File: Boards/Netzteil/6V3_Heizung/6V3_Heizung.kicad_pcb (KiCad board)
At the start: 2 copper layers, 36 parts, among them P1 6V3_AC, P2 12V_DC, P3 6V3_DC_1, P4 6V3_DC_2, Q3 IRF540N, Q4 IRF540N, U1 TL072

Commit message: Updated Layout
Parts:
- added REF**: EuroBoard_halb_Type-I_100mmX80mm_holes, EuroBoard_Outline:EuroBoard_halb_Type-I_100mmX80mm_holes, F.Cu at (59.7, 118.7)
- moved R4 42.0 mm to (110.5, 55.2), turned to 180 degrees
- moved C11 33.1 mm to (151.8, 70.5)
- moved C12 33.1 mm to (151.8, 85.7)
- moved R6 33.1 mm to (135.5, 68.3)
- moved R7 33.1 mm to (135.6, 75.2)
- moved R8 33.1 mm to (135.5, 87.9)
- moved R9 33.1 mm to (135.5, 81.3)
- moved C13 33.1 mm to (134.2, 71.6)
- moved C14 33.1 mm to (134.2, 84.6)
- moved C15 33.1 mm to (142.6, 71.6)
- moved C16 33.1 mm to (142.6, 84.6)
- moved P3 33.1 mm to (154.3, 55.9)
- moved P4 33.1 mm to (154.3, 100.3)
- moved R5 30.6 mm to (71.1, 102.2)
- moved Q4 23.7 mm to (131.4, 49.5)
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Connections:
- net Ref renamed /Reference
- net V_Unreg renamed /V_Unreg
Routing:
- net Net-(R2-Pad2): track 11.4 -> 72.9 mm
- net Net-(Q4-Pad1): track 56.5 -> 8.86 mm, vias 2 -> 0
- net Net-(C14-Pad1): track 97.1 -> 79.7 mm
- net Net-(Q3-Pad1): track 46.2 -> 59.6 mm
- net Net-(C11-Pad1): track 77.9 -> 67.7 mm
- net /Reference: track 45.2 -> 36.6 mm
- net Net-(C12-Pad1): track 75.9 -> 67.2 mm
- net /V_Unreg: track 135.3 -> 143.2 mm
- net Net-(R3-Pad2): track 19.6 -> 23.2 mm
- net Net-(C13-Pad1): track 73.0 -> 69.5 mm
- net +12V: track 53.7 -> 50.6 mm
- net Net-(C1-Pad1): track 36.6 -> 33.5 mm
- net Net-(C6-Pad1): track 6.40 -> 7.94 mm
- net Net-(C7-Pad1): track 3.81 -> 5.34 mm
- net Net-(C2-Pad2): track 32.6 -> 33.3 mm
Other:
- board outline added: 100 x 80 mm

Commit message: Work in Progress
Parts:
- moved C9 0.64 mm to (81.3, 53.3)
- turned D5 to 180 degrees
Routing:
- net GND: track 0.00 -> 20.8 mm, vias 0 -> 2
- net Net-(C13-Pad1): track 69.5 -> 66.0 mm
- net Net-(C14-Pad1): track 79.7 -> 77.1 mm
- net Net-(C12-Pad1): track 67.2 -> 65.1 mm
- net Net-(C2-Pad2): track 33.3 -> 31.4 mm
- net /Reference: track 36.6 -> 38.0 mm
- net Net-(R2-Pad2): track 72.9 -> 71.5 mm
- net +12V: track 50.6 -> 49.4 mm
- net Net-(C1-Pad1): track 33.5 -> 32.6 mm
- net Net-(C11-Pad1): track 67.7 -> 66.9 mm
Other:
- net class Default: via_dia 1 -> 1.5

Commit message: Work in Progress
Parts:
- moved R4 26.1 mm to (135.3, 63.5)
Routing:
- net /V_Unreg: track 143.1 -> 114.3 mm
- net Net-(Q4-Pad1): track 8.86 -> 22.0 mm
- net Net-(C12-Pad1): track 65.1 -> 68.2 mm
- net Net-(R2-Pad2): track 71.5 -> 69.4 mm, vias 0 -> 2
- net Net-(C13-Pad1): track 66.0 -> 67.6 mm
- net Net-(C11-Pad1): track 66.9 -> 67.9 mm
- net Net-(C14-Pad1): track 77.1 -> 76.5 mm
- added copper zone on B.Cu, net /V_Unreg

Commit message: Work in Progress
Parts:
- P2: footprint MiniUniversalMate-N-LokSockets_13Aug2012:MiniUniversalMate-N-LokSocket_2PinVertical_12Aug2012 -> Connectors_Molex:Molex_KK-6410-02_02x2.54mm_Straight
- moved R1 3.43 mm to (73.3, 88.4)
- moved R3 3.05 mm to (79.9, 102.2)
- moved R2 2.57 mm to (101.0, 100.6)
- moved D5 2.29 mm to (78.4, 88.4), turned to 90 degrees
- moved R5 2.16 mm to (73.3, 102.2)
- moved C6 1.94 mm to (97.2, 100.6)
- moved C7 1.55 mm to (83.4, 98.1)
- moved P2 0.64 mm to (64.8, 88.3)
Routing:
- net /Reference: track 38.0 -> 32.1 mm
- net GND: track 20.8 -> 26.5 mm
- net +12V: track 49.4 -> 53.6 mm
- net /V_Unreg: track 114.3 -> 111.1 mm
- net Net-(C13-Pad1): track 67.6 -> 70.0 mm
- net Net-(Q3-Pad1): track 59.6 -> 57.7 mm
- net Net-(C14-Pad1): track 76.5 -> 74.8 mm
- net Net-(R2-Pad2): track 69.4 -> 67.8 mm
- net Net-(C7-Pad1): track 5.34 -> 3.94 mm
- net Net-(C6-Pad1): track 7.69 -> 6.66 mm
- net Net-(R3-Pad2): track 23.6 -> 23.0 mm
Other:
- board text added: "Bot"
- board text added: "D. Walter v1.0"

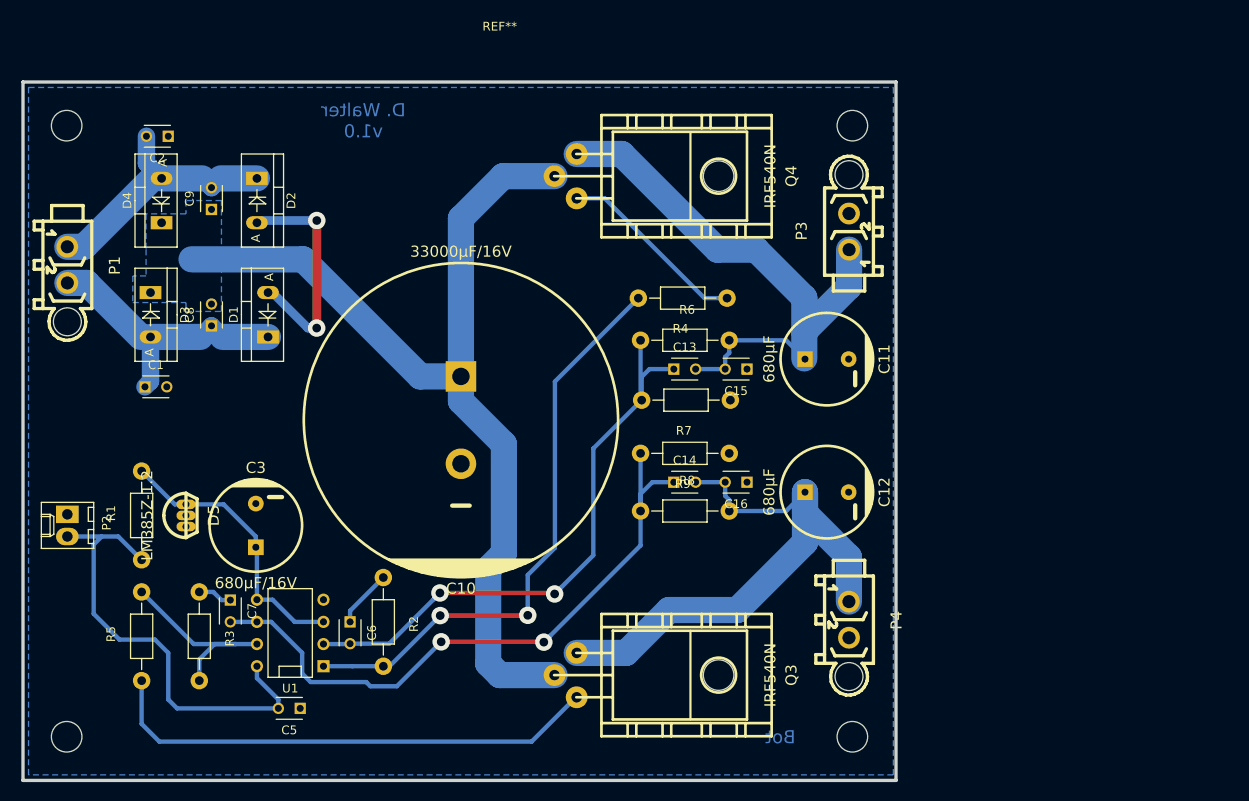
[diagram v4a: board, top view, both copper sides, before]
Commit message: Converted to Kicad 5.1 and Layout changes
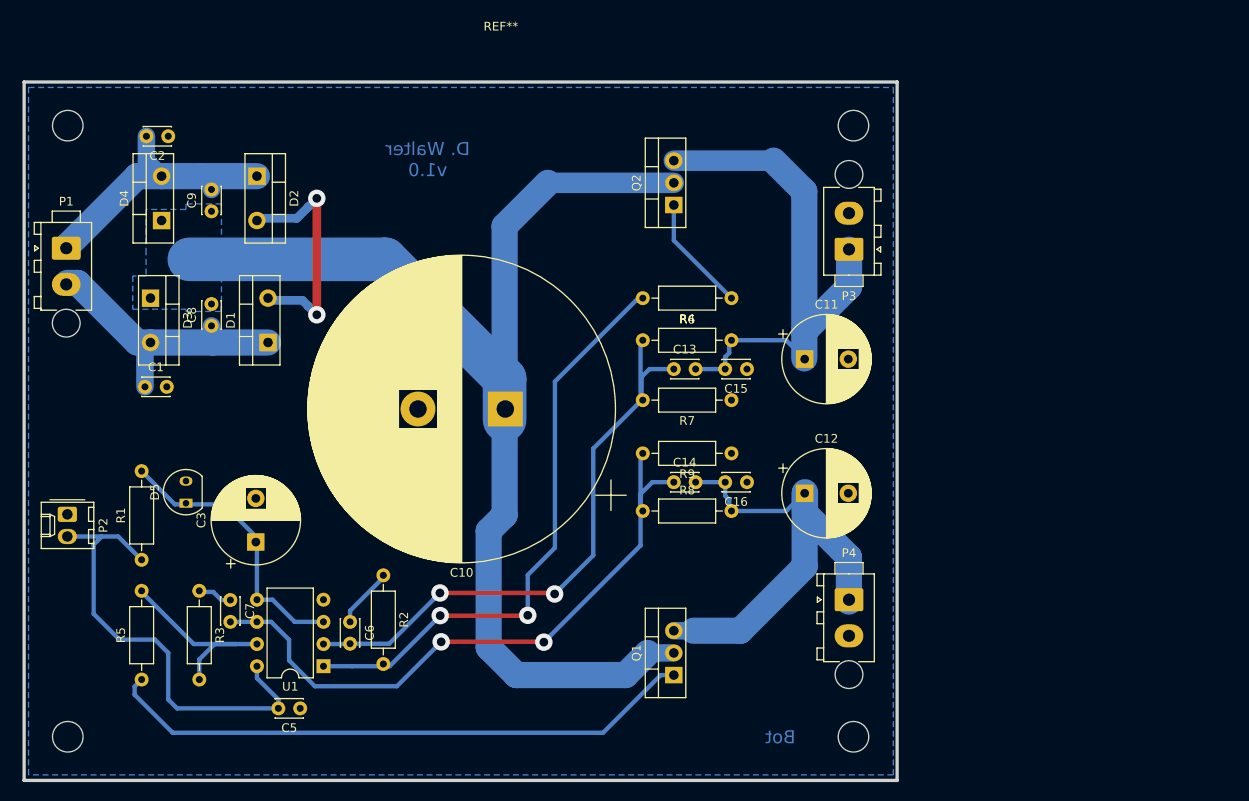
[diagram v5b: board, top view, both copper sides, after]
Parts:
- removed Q3, Q4: IRF540N, w_to:to220-horiz_5772
- added Q1: IRF540N, Package_TO_SOT_THT:TO-220-3_Vertical, F.Cu at (134.2, 106.7)
- added Q2: IRF540N, Package_TO_SOT_THT:TO-220-3_Vertical, F.Cu at (134.2, 52.8)
- C1, C13, C14, C15, C16, C2, C5, C6, C7, C8, C9: footprint Capacitors_ThroughHole:C_Disc_D3_P2.5 -> Capacitor_THT:C_Disc_D3.0mm_W2.0mm_P2.50mm
- C10: footprint w_capacitors:CP_35x40mm -> Capacitor_THT:CP_Radial_D35.0mm_P10.00mm_SnapIn
- C11, C12, C3: footprint w_capacitors:CP_10x16mm -> Capacitor_THT:CP_Radial_D10.0mm_P5.00mm
- D1, D2, D3, D4: footprint Diodes_ThroughHole:Diode_TO-220_Vertical -> Package_TO_SOT_THT:TO-220-2_Vertical
- D5: footprint w_to:to92_3_flat -> Package_TO_SOT_THT:TO-92-2
- P1, P3, P4: footprint MiniUniversalMate-N-LokSockets_13Aug2012:MiniUniversalMate-N-LokSocket_2PinVertical_12Aug2012 -> Connector_TE-Connectivity:TE_MATE-N-LOK_1-770866-x_1x02_P4.14mm_Vertical
- P2: footprint Connectors_Molex:Molex_KK-6410-02_02x2.54mm_Straight -> Connector_Molex:Molex_KK-254_AE-6410-02A_1x02_P2.54mm_Vertical
- R1, R2, R3, R4, R5, R6, R7, R8, R9: footprint Resistors_ThroughHole:Resistor_Horizontal_RM10mm -> Resistor_THT:R_Axial_DIN0207_L6.3mm_D2.5mm_P10.16mm_Horizontal
- U1: footprint Sockets_DIP:DIP-8__300 -> Package_DIP:DIP-8_W7.62mm
- moved R4 5.59 mm to (140.8, 63.5)
- moved U1 5.39 mm to (94.1, 105.7), turned to 180 degrees
- moved R2 5.33 mm to (101.0, 95.2)
- moved R9 5.33 mm to (140.8, 81.3)
- moved C10 5.24 mm to (114.9, 76.2)
- moved R3 5.21 mm to (79.9, 97.0)
- moved R7 5.21 mm to (140.8, 75.2)
- moved R1 5.08 mm to (73.3, 93.5)
- moved R5 4.95 mm to (73.3, 107.2)
- moved R6 4.83 mm to (130.7, 68.3)
- moved R8 4.83 mm to (130.7, 87.9)
- moved C12 2.54 mm to (149.2, 85.9), turned to 0 degrees
- moved C11 2.54 mm to (149.2, 70.5), turned to 0 degrees
- moved P4 2.29 mm to (154.3, 98.0), turned to 0 degrees
- moved P3 2.03 mm to (154.3, 57.9), turned to 180 degrees
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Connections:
- U1 pad 8: +12V -> (no net)
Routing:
- net /V_Unreg: track 111.1 -> 140.6 mm
- net Net-(C12-Pad1): track 68.2 -> 57.5 mm
- net Net-(Q1-Pad1): track 57.7 -> 68.4 mm
- net Net-(Q2-Pad1): track 22.0 -> 13.4 mm
- net Net-(C11-Pad1): track 67.9 -> 63.6 mm
- net Net-(C2-Pad2): track 31.4 -> 32.7 mm
- net GND: track 26.5 -> 27.7 mm
- net Net-(C1-Pad1): track 32.6 -> 33.1 mm

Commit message: Minor Layout changes
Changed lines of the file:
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@@
     (thickness 1.6)
     (drawings 2)
-    (tracks 170)
+    (tracks 172)
     (zones 0)
     (modules 37)
@@
   (segment (start 149.18448 67.31) (end 149.18448 51.26748) (width 3) (layer B.Cu) (net 9))
   (segment (start 145.669 47.752) (end 149.18448 51.26748) (width 3) (layer B.Cu) (net 9))
-  (segment (start 134.239 47.752) (end 145.669 47.752) (width 2.35) (layer B.Cu) (net 9))
+  (segment (start 136.652 47.752) (end 145.669 47.752) (width 3) (layer B.Cu) (net 9))
+  (segment (start 134.239 47.752) (end 136.652 47.752) (width 2.35) (layer B.Cu) (net 9))
   (segment (start 140.121 84.582) (end 140.121 86.15318) (width 0.5) (layer B.Cu) (net 10))
   (segment (start 140.121 86.15318) (end 140.584902 86.617082) (width 0.5) (layer B.Cu) (net 10))
@@
   (segment (start 114.855 55.2488) (end 114.855 77.47) (width 3) (layer B.Cu) (net 14))
   (segment (start 119.8118 50.292) (end 114.855 55.2488) (width 3) (layer B.Cu) (net 14))
-  (segment (start 134.239 50.292) (end 119.8118 50.292) (width 2.35) (layer B.Cu) (net 14))
   (segment (start 114.855 77.47) (end 114.855 88.345) (width 3) (layer B.Cu) (net 14))
   (segment (start 114.855 88.345) (end 113.03 90.17) (width 3) (layer B.Cu) (net 14))
@@
   (segment (start 134.239 104.14) (end 131.239 104.14) (width 2) (layer B.Cu) (net 14))
   (segment (start 131.239 104.14) (end 128.699 106.68) (width 3) (layer B.Cu) (net 14))
+  (segment (start 131.064 50.292) (end 119.8118 50.292) (width 3) (layer B.Cu) (net 14))
+  (segment (start 134.239 50.292) (end 131.064 50.292) (width 2.35) (layer B.Cu) (net 14))
   (segment (start 72.479001 107.987999) (end 72.479001 108.928001) (width 0.5) (layer B.Cu) (net 15))
   (segment (start 73.279 107.188) (end 72.479001 107.987999) (width 0.5) (layer B.Cu) (net 15))

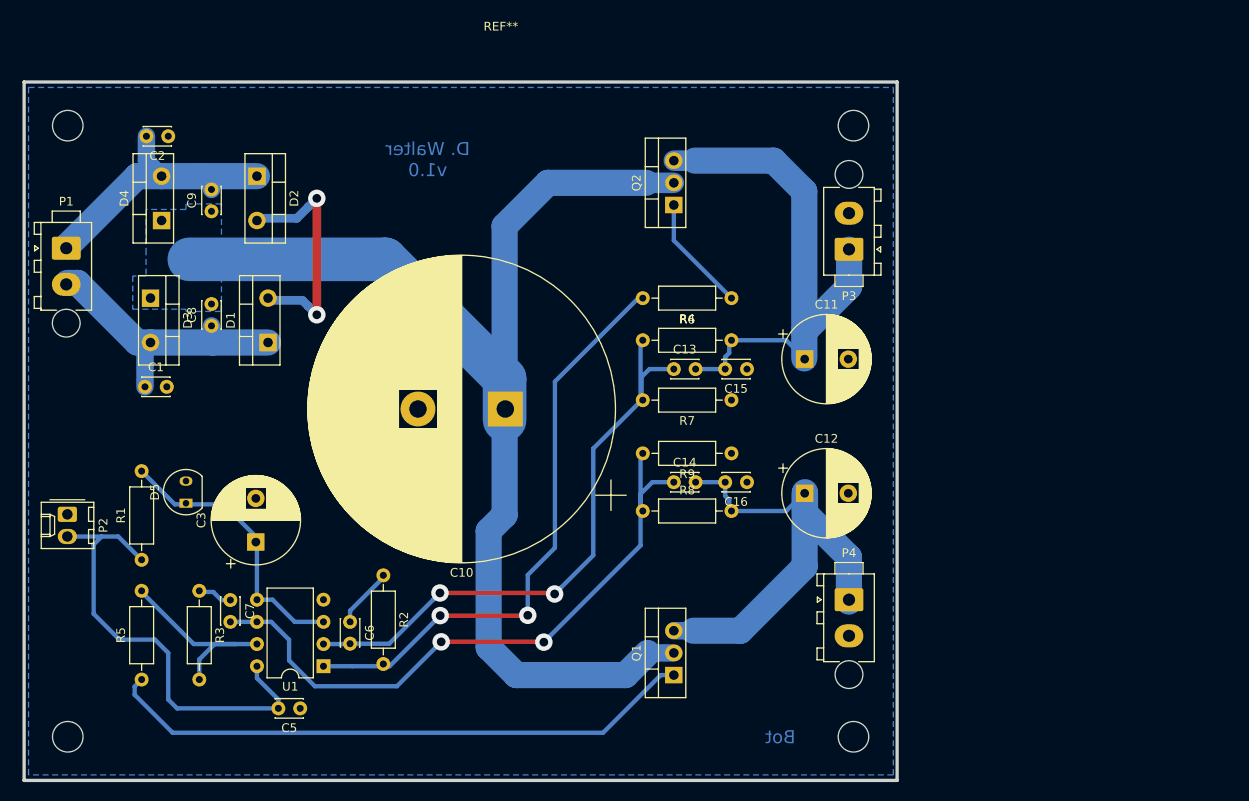
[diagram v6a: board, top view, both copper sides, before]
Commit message: Layout changes, Supply connector changes, Mounting holes
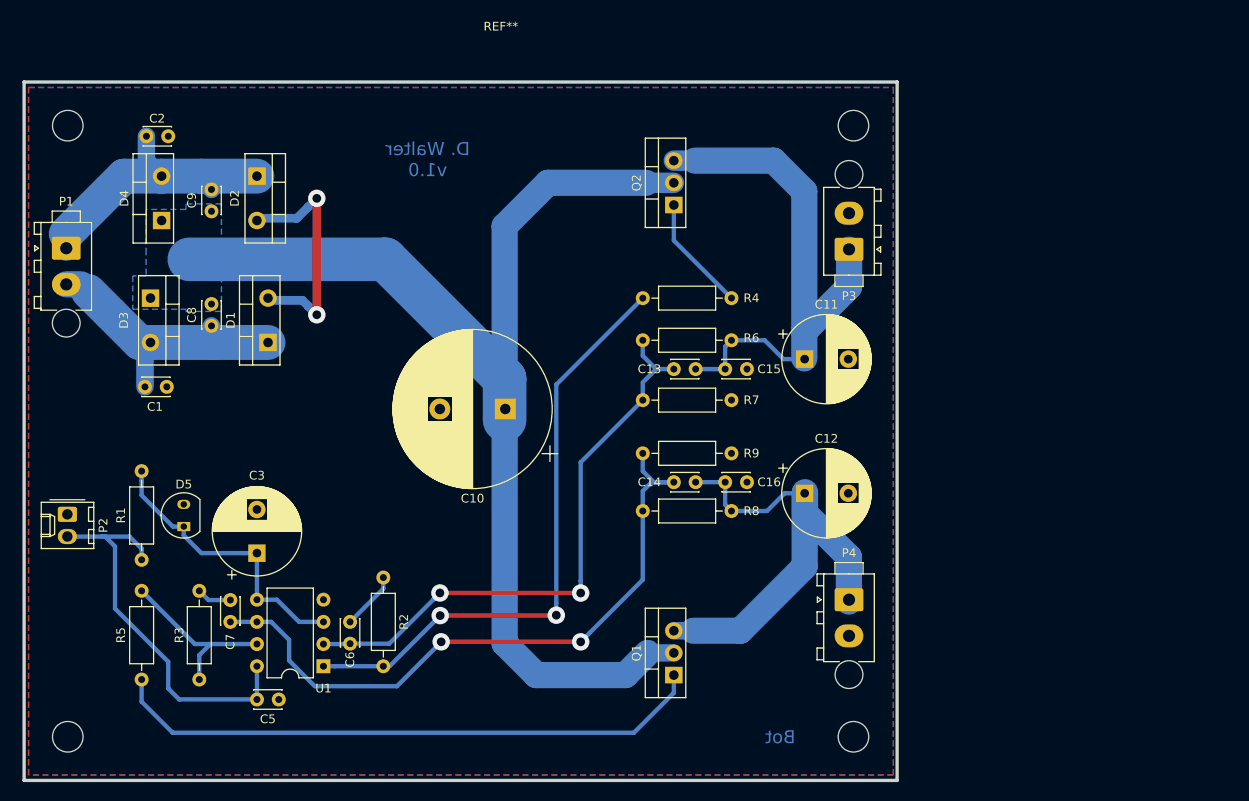
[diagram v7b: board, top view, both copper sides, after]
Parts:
- C10: footprint Capacitor_THT:CP_Radial_D35.0mm_P10.00mm_SnapIn -> Capacitor_THT:CP_Radial_D18.0mm_P7.50mm
- P1: value 6V3_AC -> 7V5_AC
- moved D5 2.68 mm to (78.1, 89.7)
- moved C5 2.66 mm to (89.0, 109.5)
- moved C3 1.28 mm to (86.5, 92.7)
- moved R2 0.25 mm to (101.0, 95.5)
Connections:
- U1 pad 8: (no net) -> +12V
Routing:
- net +12V: track 53.6 -> 45.4 mm
- net /V_Unreg: track 140.6 -> 137.7 mm
- net Net-(R3-Pad2): track 23.0 -> 20.3 mm
- net Net-(C14-Pad1): track 74.8 -> 77.3 mm
- net Net-(R2-Pad2): track 67.8 -> 69.9 mm
- net Net-(C1-Pad1): track 33.1 -> 31.1 mm
- net Net-(C13-Pad1): track 70.0 -> 68.3 mm
- net /Reference: track 32.1 -> 33.5 mm
- net Net-(C2-Pad2): track 32.7 -> 33.8 mm
- net Net-(Q1-Pad1): track 68.4 -> 68.9 mm
- added copper zone on F.Cu, net GND
